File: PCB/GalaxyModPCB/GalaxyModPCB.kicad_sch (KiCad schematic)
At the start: 42 parts, among them J1 LED RGBW Connector, J2 USB to UART, Q1 IRLML0030, Q2 IRLML0030, Q3 IRLML0030, Q4 IRLML0030, U1 ESP32-WROOM-32, U2 AMS1117-3.3

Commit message: First draft drawn
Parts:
- removed M?: Motor_DC, symbol Motor:Motor_DC
- added D?: 1N4004, Diode_THT:D_DO-41_SOD81_P10.16mm_Horizontal, symbol Diode:1N4004
- added J3: Motor Connector, symbol Connector_Generic:Conn_01x02
- added J4: Projector Connector, Connector_JST:JST_VH_B2P-VH-B_1x02_P3.96mm_Vertical, symbol Connector_Generic:Conn_01x02
- added Q5, Q?: IRLML0030, Package_TO_SOT_SMD:SOT-23, symbol Transistor_FET:IRLML0030
- added R? (x2): 100K, Resistor_SMD:R_0805_2012Metric_Pad1.20x1.40mm_HandSolder, symbol Device:R_Small
- added R? (x2): 1K, Resistor_SMD:R_0805_2012Metric_Pad1.20x1.40mm_HandSolder, symbol Device:R_Small
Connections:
- net GNDREF: now also Q5.3 (D), Q?.3 (D), R?.1, R?.1
- net VCC: now also D?.1 (K), J3.1 (Pin_1), J4.1 (Pin_1)
- net at U1.33 (IO21): now also R?.2, R?.2
- net at U1.36 (IO22): now also R?.2, R?.2
- new net: Q5.1 (G), R?.1
- new net: D?.2 (A), J3.2 (Pin_2), Q5.2 (S)
- new net: J4.2 (Pin_2), Q?.2 (S)

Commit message: Labelled and named
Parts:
- removed R27: 10K, Resistor_SMD:R_0805_2012Metric_Pad1.20x1.40mm_HandSolder, symbol Device:R_Small
- added C3: 22uF/10V(20%), symbol Device:C
- gave numbers to parts that had none: 6
- renumbered C3 to C4
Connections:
- net GNDREF: now also C2.1, C3.1; no longer C2.2
- net at C1.1, R27.2, U1.2 (VDD): now also C2.2, U1.3 (EN), C3.2
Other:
- note added: "Galaxy Projector Mod"
- moved on the sheet: C2

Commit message: Added switches
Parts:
- added C5, C6, C7, C8: 0.1uF, symbol Device:C
- added R34, R35, R36, R37: 10K, Resistor_SMD:R_0805_2012Metric_Pad1.20x1.40mm_HandSolder, symbol Device:R_Small
- added SW1: On/Off, symbol Switch:SW_Push
- added SW2: Colour, symbol Switch:SW_Push
- added SW3: Brightness, symbol Switch:SW_Push
- added SW4: Motor, symbol Switch:SW_Push
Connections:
- net +3.3V: now also J4.1 (Pin_1), C5.2, C6.2, C7.2, C8.2, SW1.2, SW2.2, SW3.2, SW4.2
- net GNDREF: now also R34.1, R35.1, R36.1, R37.1
- net VCC: no longer J4.1 (Pin_1)
- net at U1.10 (IO25): now also C6.1, R36.2, SW2.1
- net at U1.11 (IO26): now also C7.1, R35.2, SW3.1
- net at U1.12 (IO27): now also C8.1, R34.2, SW4.1
- net at U1.37 (IO23): now also C5.1, R37.2, SW1.1
- net at Q6.1 (G): now also R30.1
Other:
- moved on the sheet: J4, Q6, R30, R31, U1

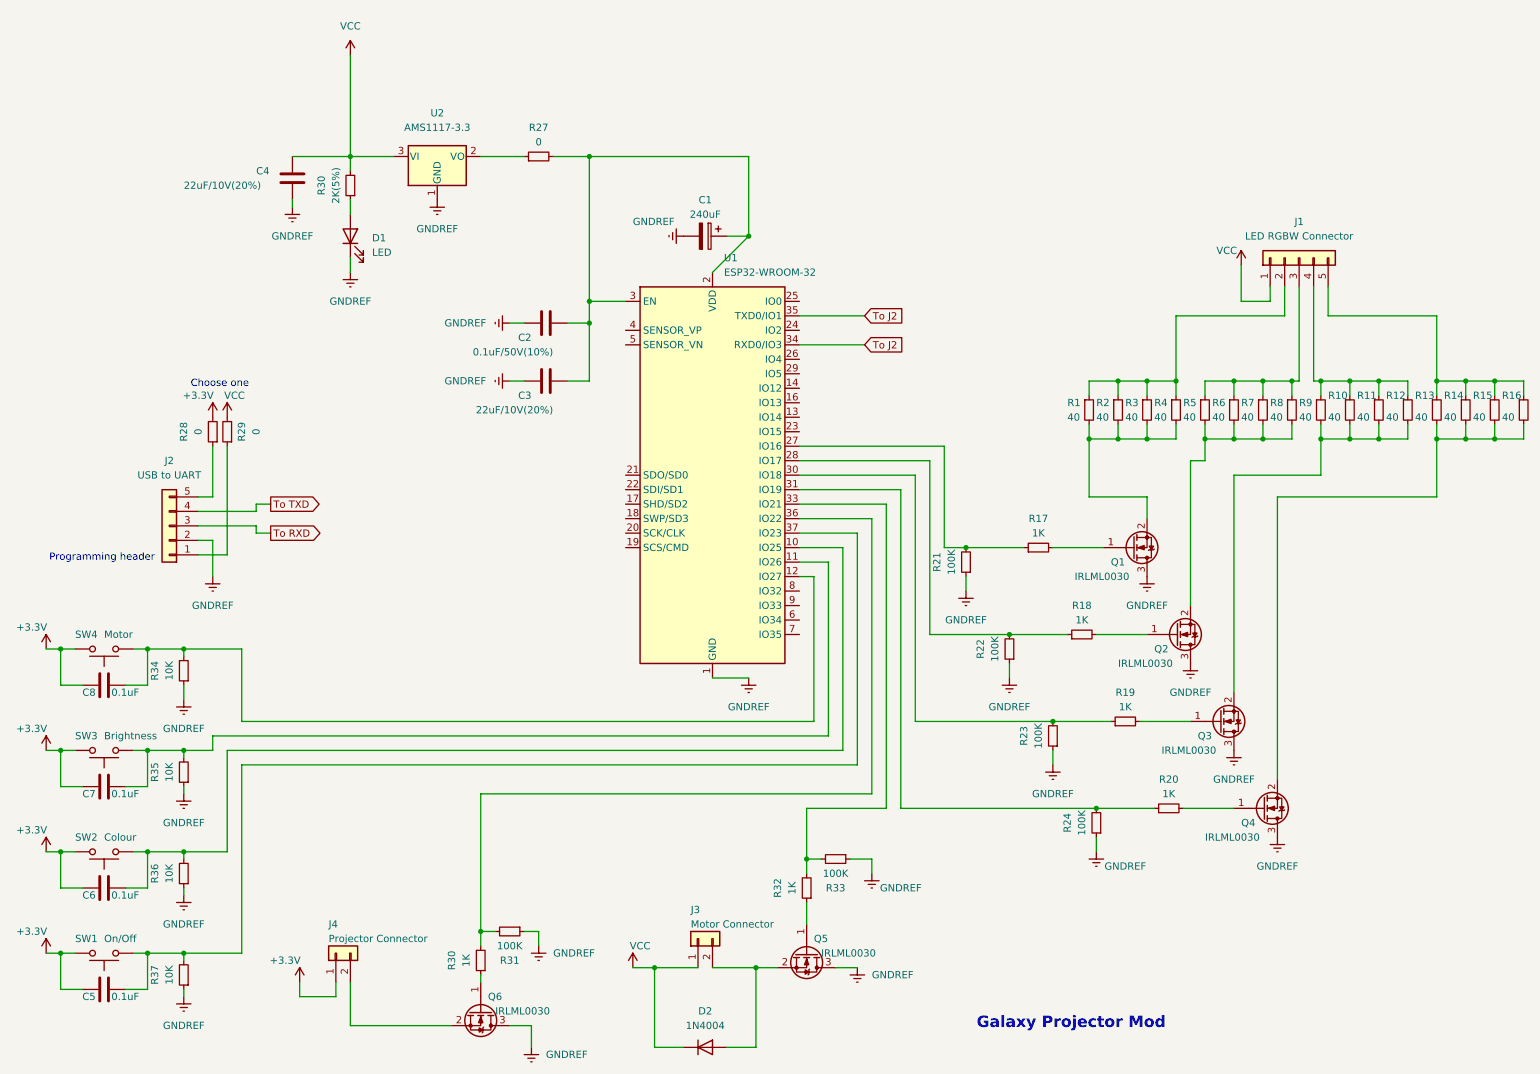
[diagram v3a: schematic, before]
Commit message: Added debugging header
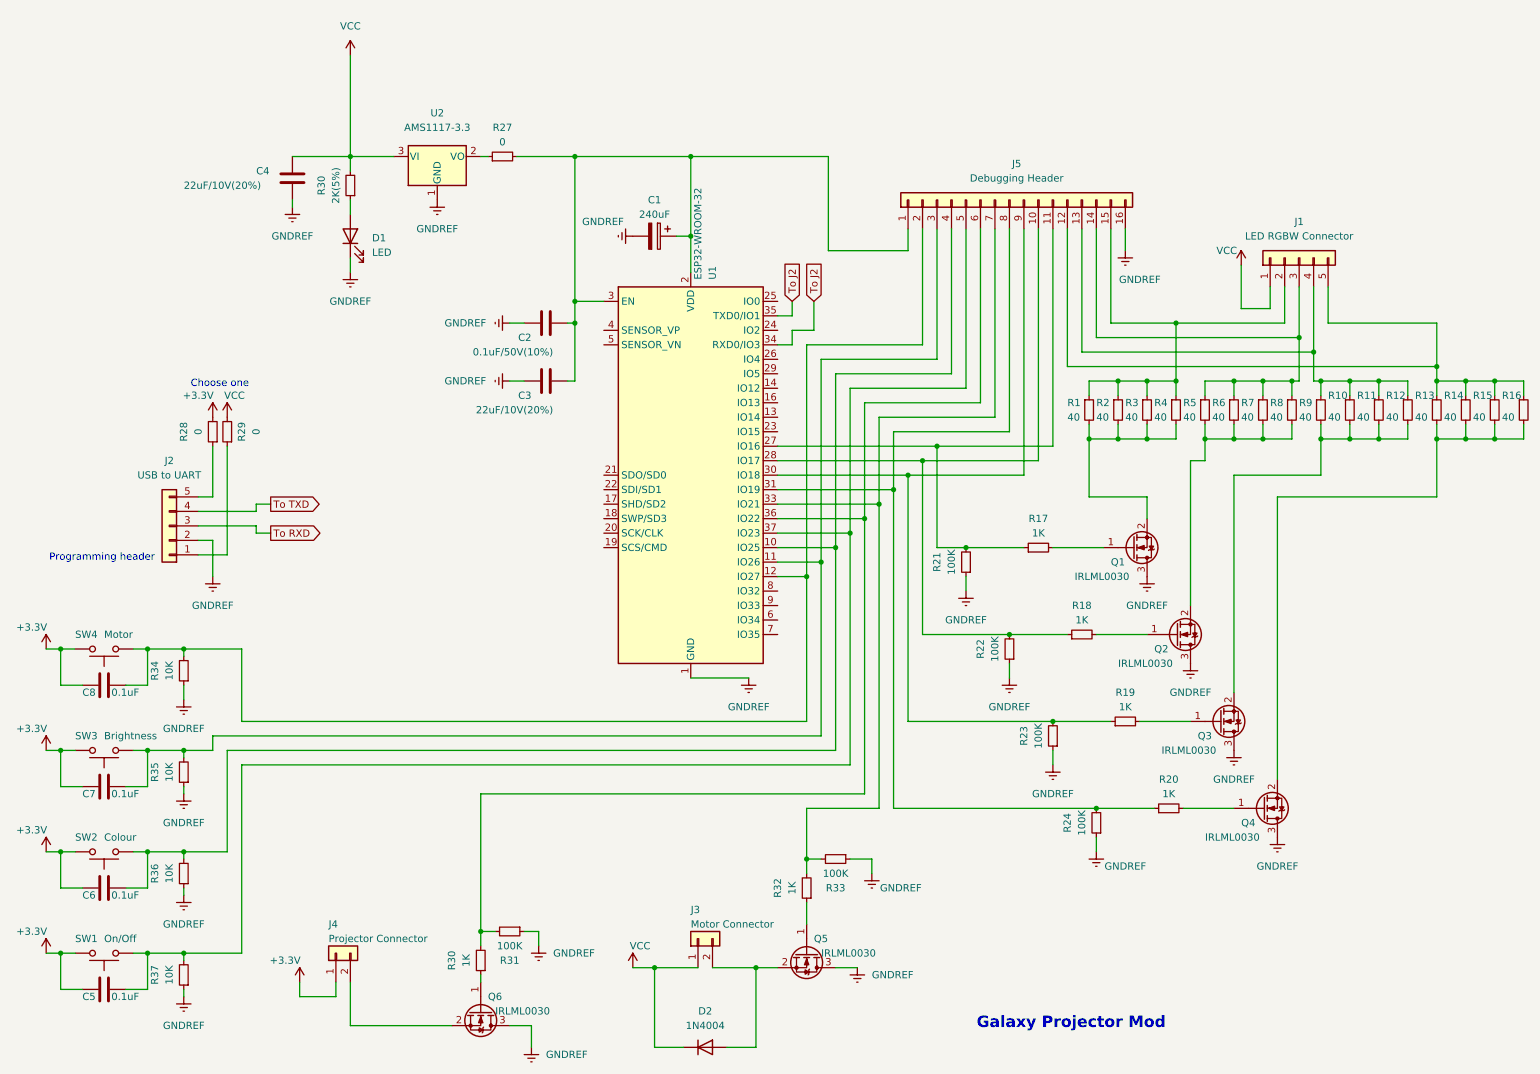
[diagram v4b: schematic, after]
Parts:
- added J5: Debugging Header, symbol Connector_Generic:Conn_01x16
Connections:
- net GNDREF: now also J5.16 (Pin_16)
- net at R19.1, R23.2, U1.30 (IO18): now also J5.9 (Pin_9)
- net at C6.1, R36.2, SW2.1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: now also J5.4 (Pin_4)
- net at C7.1, R35.2, SW3.1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: now also J5.3 (Pin_3)
- net at C8.1, R34.2, SW4.1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: now also J5.2 (Pin_2)
- net at C1.1, C2.2, C3.2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: now also J5.1 (Pin_1)
- net at R17.1, R21.2, U1.27 (IO16): now also J5.11 (Pin_11)
- net at R18.1, R22.2, U1.28 (IO17): now also J5.10 (Pin_10)
- net at R20.1, R24.2, U1.31 (IO19): now also J5.8 (Pin_8)
- net at R32.2, R33.2, U1.33 (IO21): now also J5.7 (Pin_7)
- net at R30.2, R31.2, U1.36 (IO22): now also J5.6 (Pin_6)
- net at C5.1, R37.2, SW1.1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: now also J5.5 (Pin_5)
- net at J1.4 (Pin_4), R10.1, R11.1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: now also J5.13 (Pin_13)
- net at J1.2 (Pin_2), R1.1, R2.1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: now also J5.15 (Pin_15)
- net at J1.3 (Pin_3), R5.1, R6.1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: now also J5.14 (Pin_14)
- net at J1.5 (Pin_5), R13.1, R14.1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: now also J5.12 (Pin_12)
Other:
- moved on the sheet: C1, R27, U1

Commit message: Fixed annotations
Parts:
- renumbered R30 to R31, R31 to R32, R32 to R33, R33 to R34, R34 to R35, R35 to R36, R36 to R37, R37 to R38

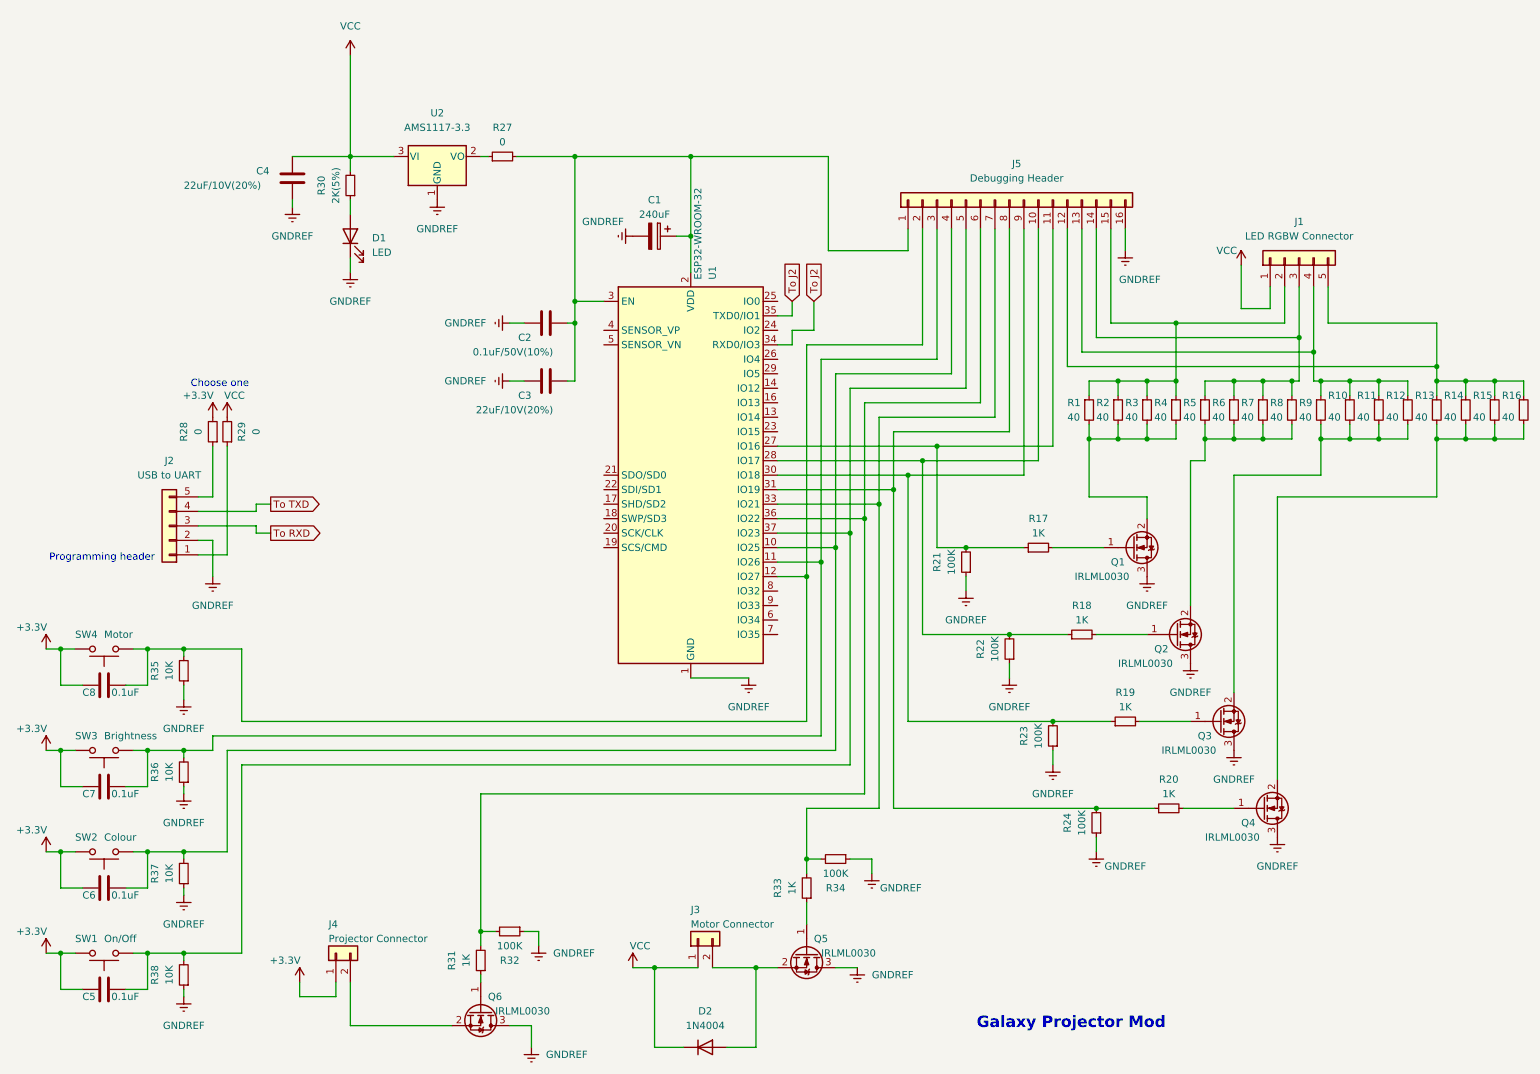
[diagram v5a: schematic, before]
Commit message: Fixed connector footprints
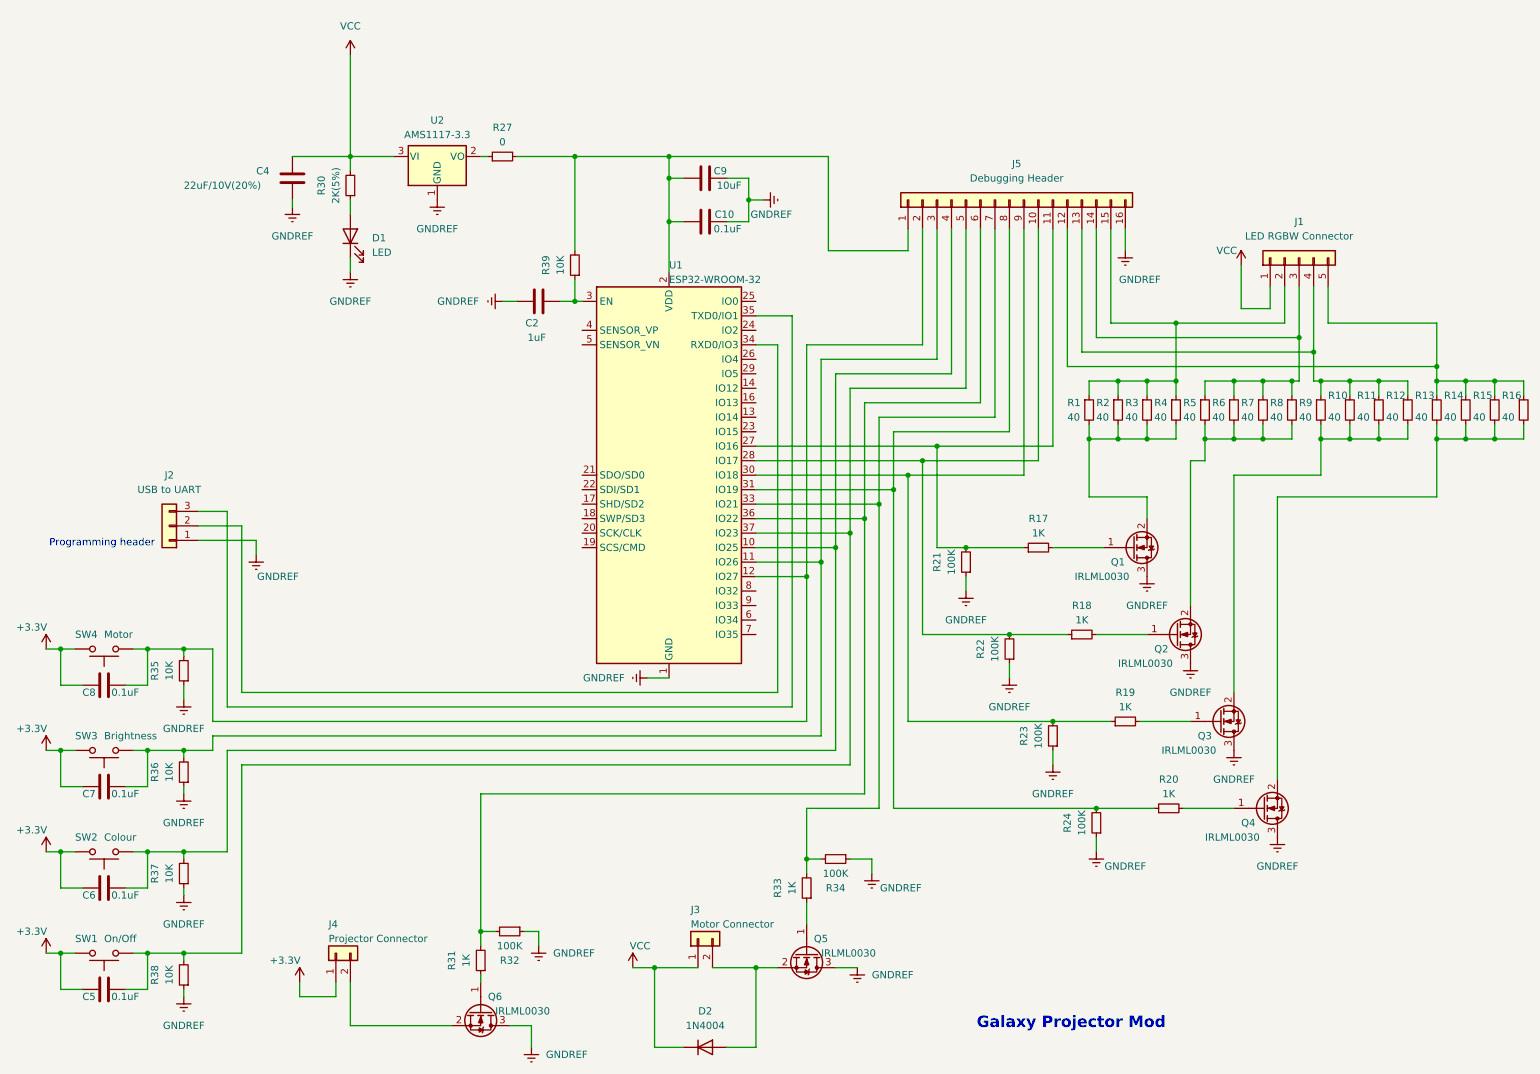
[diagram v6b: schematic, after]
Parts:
- removed C1: 240uF, Capacitor_THT:CP_Radial_D4.0mm_P1.50mm, symbol Device:C_Polarized
- removed C3: 22uF/10V(20%), symbol Device:C
- removed J2: USB to UART, Connector_JST:JST_VH_B5P-VH-B_1x05_P3.96mm_Vertical, symbol Connector_Generic:Conn_01x05
- removed R28, R29: 0, Resistor_SMD:R_0805_2012Metric_Pad1.20x1.40mm_HandSolder, symbol Device:R_Small
- added C10: 0.1uF, symbol Device:C
- added C9: 10uF, symbol Device:C
- added J2: USB to UART, symbol Connector_Generic:Conn_01x03
- added R39: 10K, Resistor_SMD:R_0805_2012Metric_Pad1.20x1.40mm_HandSolder, symbol Device:R_Small
- C2: value 0.1uF/50V(10%) -> 1uF
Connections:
- net GNDREF: now also C10.2, C9.2, J2.1 (Pin_1)
- net at J5.1 (Pin_1), R27.2, U1.2 (VDD): now also C10.1, C9.1, R39.2; no longer C2.2, U1.3 (EN)
- net To J2: no longer names the net of U1.34 (RXD0/IO3)
- net To J2: now also J2.2 (Pin_2); no longer U1.35 (TXD0/IO1)
- new net: C2.2, R39.1, U1.3 (EN)
- new net: J2.3 (Pin_3), U1.35 (TXD0/IO1)
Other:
- note removed: "Choose one"
- moved on the sheet: C2, U1

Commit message: Added power connector
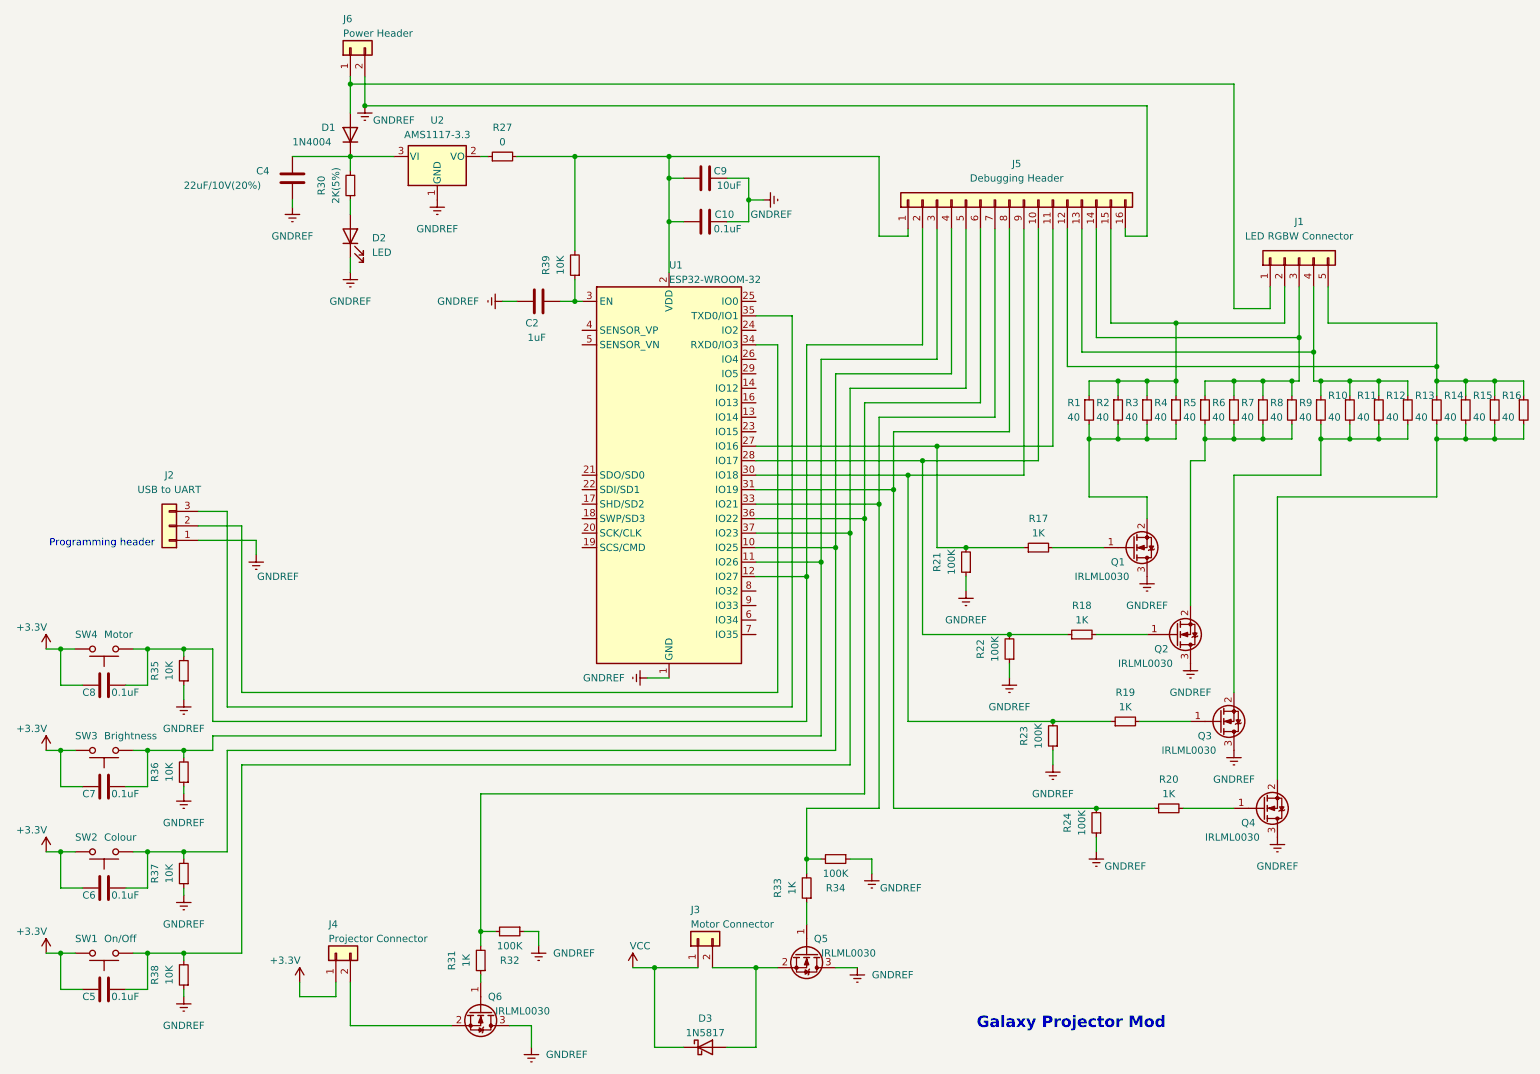
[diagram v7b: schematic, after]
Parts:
- removed D2: 1N4004, Diode_THT:D_DO-41_SOD81_P10.16mm_Horizontal, symbol Diode:1N4004
- added D1: 1N4004, Diode_THT:D_DO-41_SOD81_P10.16mm_Horizontal, symbol Diode:1N4004
- added D3: 1N5817, Diode_THT:D_DO-41_SOD81_P10.16mm_Horizontal, symbol Diode:1N5817
- added J6: Power Header, Connector_JST:JST_VH_B2P-VH-B_1x02_P3.96mm_Vertical, symbol Connector_Generic:Conn_01x02
- renumbered D1 to D2
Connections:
- net GNDREF: now also J6.2 (Pin_2)
- net VCC: now also D3.1 (K); no longer C4.1, J1.1 (Pin_1), R30.2, U2.3 (VI)
- net at J3.2 (Pin_2), Q5.2 (S): now also D3.2 (A)
- new net: D1.2 (A), J1.1 (Pin_1), J6.1 (Pin_1)
- new net: C4.1, D1.1 (K), R30.2, U2.3 (VI)
